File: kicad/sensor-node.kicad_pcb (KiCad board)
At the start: 2 copper layers, 30 x 54 mm, 24 parts

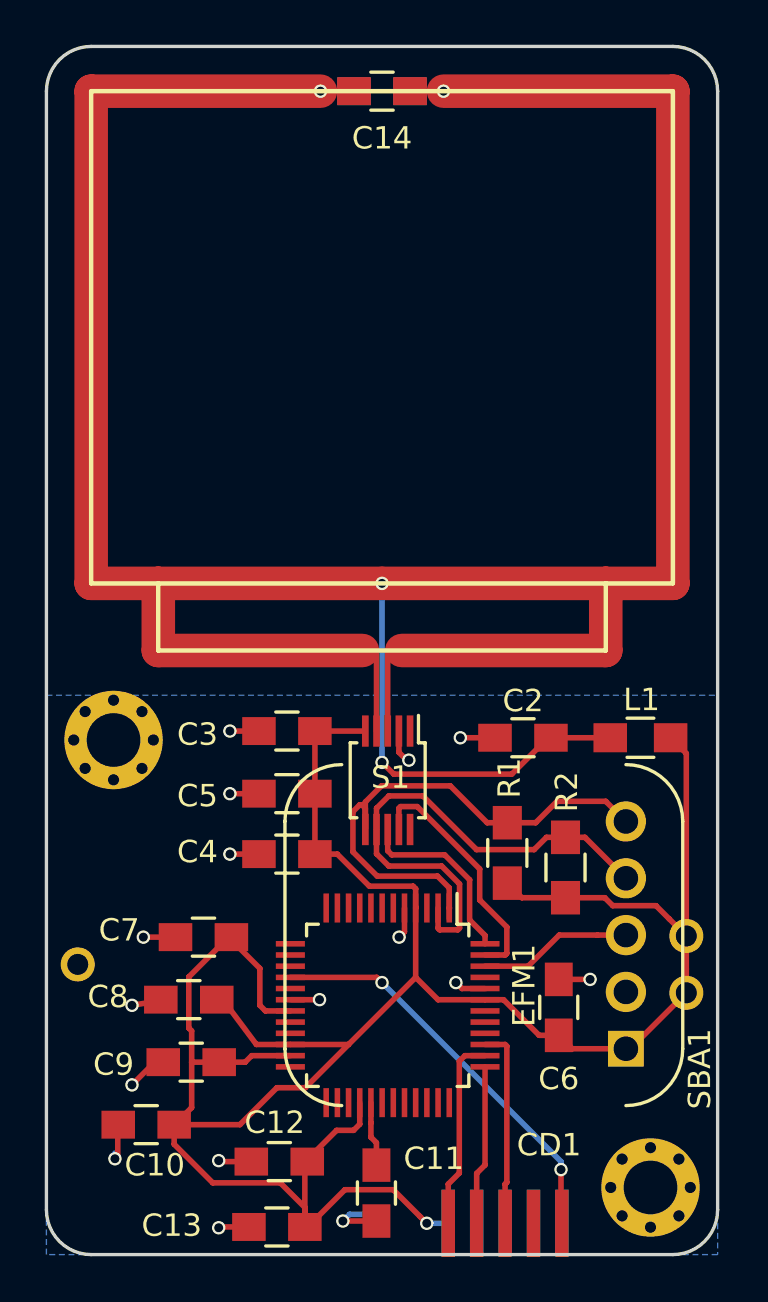
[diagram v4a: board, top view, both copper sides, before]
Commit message: rounded antenna edges
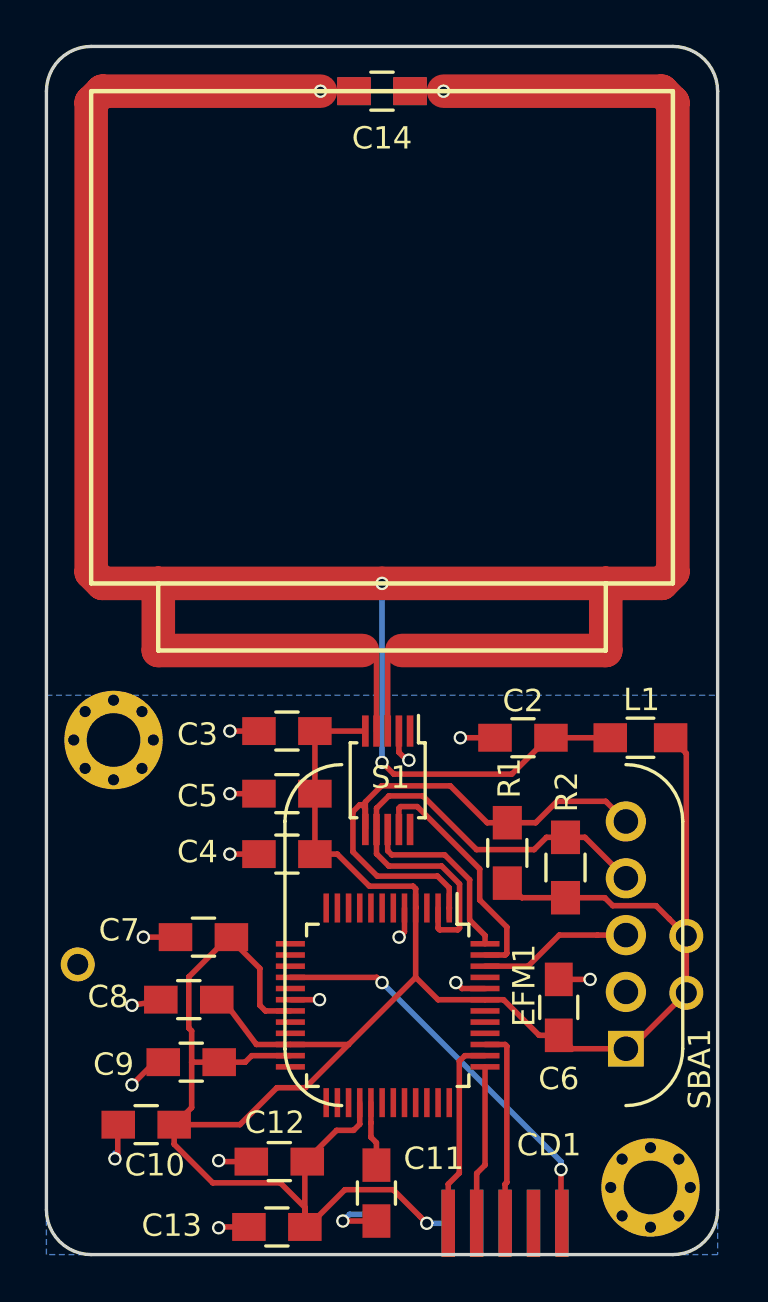
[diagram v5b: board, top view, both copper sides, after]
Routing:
- net Net-(C1-Pad1): track 148.3 -> 147.1 mm
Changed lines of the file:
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@@
     (thickness 1.6)
     (drawings 18)
-    (tracks 238)
+    (tracks 242)
     (zones 0)
     (modules 24)
@@
   (segment (start 142.367 102.87) (end 141.986 102.87) (width 0.25) (layer F.Cu) (net 2))
   (segment (start 141.986 102.87) (end 140.97 103.886) (width 0.25) (layer F.Cu) (net 2))
+  (segment (start 164.646 81.471) (end 165.146 80.971) (width 1.5) (layer F.Cu) (net 3))
+  (segment (start 165.146 59.971) (end 164.646 59.471) (width 1.5) (layer F.Cu) (net 3))
+  (segment (start 139.646 81.471) (end 139.146 80.971) (width 1.5) (layer F.Cu) (net 3))
+  (segment (start 139.146 59.971) (end 139.646 59.471) (width 1.5) (layer F.Cu) (net 3))
   (segment (start 162.346 88.371) (end 159.696 88.371) (width 0.25) (layer F.Cu) (net 3))
   (segment (start 152.4 84.475) (end 153.025 84.475) (width 0.25) (layer F.Cu) (net 3))
@@
   (segment (start 151.9 84.475) (end 151.275 84.475) (width 0.25) (layer F.Cu) (net 3))
   (segment (start 151.275 84.475) (end 151.271 84.471) (width 0.25) (layer F.Cu) (net 3))
-  (segment (start 139.146 59.471) (end 149.396 59.471) (width 1.5) (layer F.Cu) (net 3))
+  (segment (start 139.646 59.471) (end 149.396 59.471) (width 1.5) (layer F.Cu) (net 3))
   (segment (start 149.396 59.471) (end 150.896 59.471) (width 0.25) (layer F.Cu) (net 3))
   (segment (start 150.896 59.471) (end 149.396 59.471) (width 0.25) (layer B.Cu) (net 3))
   (via (at 149.396 59.471) (size 0.6) (drill 0.4) (layers F.Cu B.Cu) (net 3))
-  (segment (start 165.146 59.471) (end 154.896 59.471) (width 1.5) (layer F.Cu) (net 3))
+  (segment (start 164.646 59.471) (end 154.896 59.471) (width 1.5) (layer F.Cu) (net 3))
   (segment (start 154.896 59.471) (end 153.396 59.471) (width 0.25) (layer F.Cu) (net 3))
   (segment (start 153.396 59.471) (end 154.896 59.471) (width 0.25) (layer B.Cu) (net 3))
@@
   (segment (start 152.671001 89.996001) (end 152.146 89.471) (width 0.25) (layer F.Cu) (net 3))
   (via (at 152.146 89.471) (size 0.6) (drill 0.4) (layers F.Cu B.Cu) (net 3))
-  (segment (start 139.146 81.471) (end 139.146 59.471) (width 1.5) (layer F.Cu) (net 3))
-  (segment (start 142.146 81.471) (end 139.146 81.471) (width 1.5) (layer F.Cu) (net 3))
-  (segment (start 165.146 81.471) (end 165.146 59.471) (width 1.5) (layer F.Cu) (net 3))
-  (segment (start 162.146 81.471) (end 165.146 81.471) (width 1.5) (layer F.Cu) (net 3))
+  (segment (start 139.146 80.971) (end 139.146 59.971) (width 1.5) (layer F.Cu) (net 3))
+  (segment (start 142.146 81.471) (end 139.646 81.471) (width 1.5) (layer F.Cu) (net 3))
+  (segment (start 165.146 80.971) (end 165.146 59.971) (width 1.5) (layer F.Cu) (net 3))
+  (segment (start 162.146 81.471) (end 164.646 81.471) (width 1.5) (layer F.Cu) (net 3))
   (segment (start 162.146 84.471) (end 162.146 81.471) (width 1.5) (layer F.Cu) (net 3))
   (segment (start 153.029 84.471) (end 162.146 84.471) (width 1.5) (layer F.Cu) (net 3))

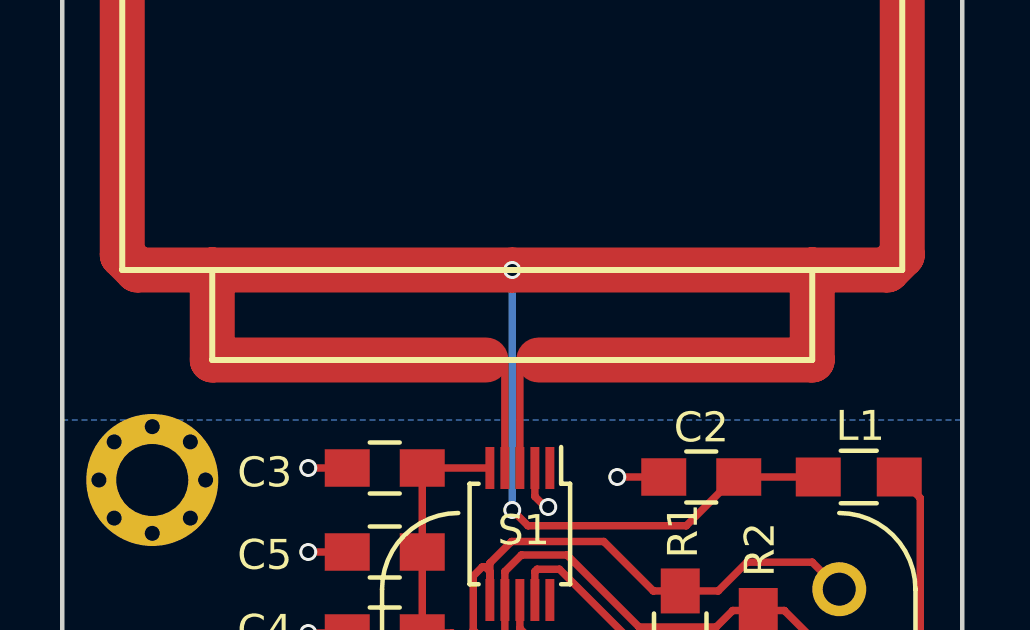
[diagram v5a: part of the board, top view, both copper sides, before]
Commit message: refined feed loop size
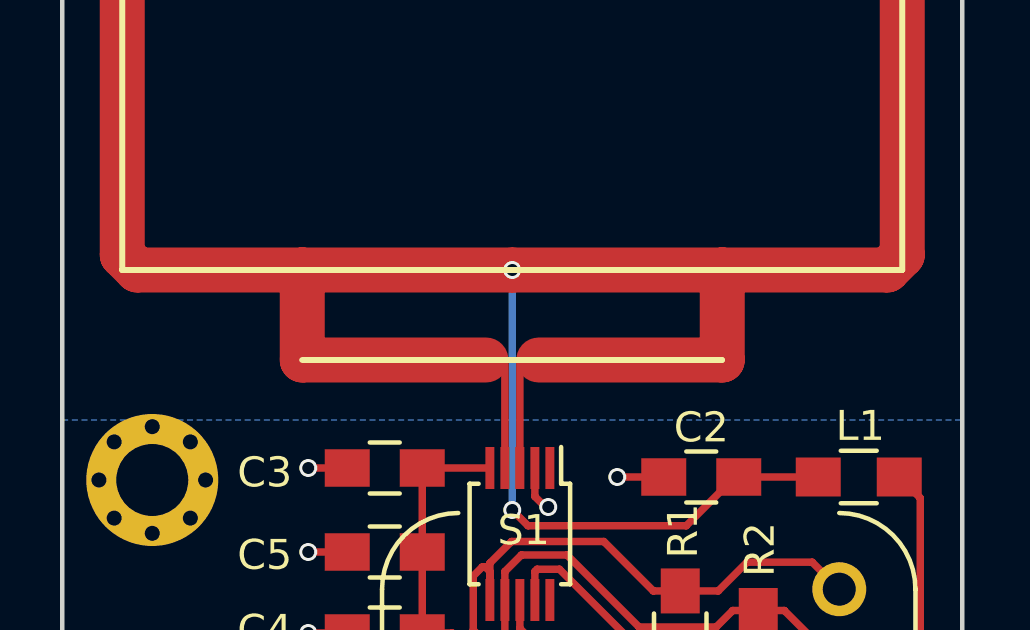
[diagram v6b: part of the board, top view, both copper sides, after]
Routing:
- net Net-(C1-Pad1): track 147.1 -> 141.1 mm
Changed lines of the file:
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@@
     (area 124.24918 56.396 179.995999 119.171001)
     (thickness 1.6)
-    (drawings 18)
+    (drawings 16)
     (tracks 242)
     (zones 0)
@@
     (arrow2b (pts (xy 172.145999 57.471) (xy 172.73242 58.597504)))
   )
-  (gr_line (start 142.146 84.471) (end 142.146 81.471) (layer F.SilkS) (width 0.2))
-  (gr_line (start 162.146 84.471) (end 142.146 84.471) (layer F.SilkS) (width 0.2))
-  (gr_line (start 162.146 81.471) (end 162.146 84.471) (layer F.SilkS) (width 0.2))
+  (gr_line (start 159.146 84.471) (end 145.146 84.471) (layer F.SilkS) (width 0.2))
   (gr_line (start 139.146 81.471) (end 139.146 59.471) (layer F.SilkS) (width 0.2))
   (gr_line (start 165.146 81.471) (end 139.146 81.471) (layer F.SilkS) (width 0.2))
@@
   (segment (start 153.396 59.471) (end 154.896 59.471) (width 0.25) (layer B.Cu) (net 3))
   (via (at 154.896 59.471) (size 0.6) (drill 0.4) (layers F.Cu B.Cu) (net 3))
-  (segment (start 142.146 81.471) (end 152.146 81.471) (width 1.5) (layer F.Cu) (net 3))
-  (segment (start 152.146 81.471) (end 162.146 81.471) (width 1.5) (layer F.Cu) (net 3))
+  (segment (start 145.146 81.471) (end 152.146 81.471) (width 1.5) (layer F.Cu) (net 3))
+  (segment (start 152.146 81.471) (end 159.146 81.471) (width 1.5) (layer F.Cu) (net 3))
   (segment (start 152.146 89.471) (end 152.146 81.471) (width 0.25) (layer B.Cu) (net 3))
   (via (at 152.146 81.471) (size 0.6) (drill 0.4) (layers F.Cu B.Cu) (net 3))
@@
   (via (at 152.146 89.471) (size 0.6) (drill 0.4) (layers F.Cu B.Cu) (net 3))
   (segment (start 139.146 80.971) (end 139.146 59.971) (width 1.5) (layer F.Cu) (net 3))
-  (segment (start 142.146 81.471) (end 139.646 81.471) (width 1.5) (layer F.Cu) (net 3))
+  (segment (start 145.146 81.471) (end 139.646 81.471) (width 1.5) (layer F.Cu) (net 3))
   (segment (start 165.146 80.971) (end 165.146 59.971) (width 1.5) (layer F.Cu) (net 3))
-  (segment (start 162.146 81.471) (end 164.646 81.471) (width 1.5) (layer F.Cu) (net 3))
-  (segment (start 162.146 84.471) (end 162.146 81.471) (width 1.5) (layer F.Cu) (net 3))
-  (segment (start 153.029 84.471) (end 162.146 84.471) (width 1.5) (layer F.Cu) (net 3))
+  (segment (start 159.146 81.471) (end 164.646 81.471) (width 1.5) (layer F.Cu) (net 3))
+  (segment (start 159.146 84.471) (end 159.146 81.471) (width 1.5) (layer F.Cu) (net 3))
+  (segment (start 153.029 84.471) (end 159.146 84.471) (width 1.5) (layer F.Cu) (net 3))
   (segment (start 152.4 84.475) (end 152.404 84.471) (width 0.25) (layer F.Cu) (net 3))
   (segment (start 152.4 88.071) (end 152.4 84.475) (width 0.25) (layer F.Cu) (net 3))
-  (segment (start 142.146 84.471) (end 142.146 81.471) (width 1.5) (layer F.Cu) (net 3))
-  (segment (start 151.271 84.471) (end 142.146 84.471) (width 1.5) (layer F.Cu) (net 3))
+  (segment (start 145.146 84.471) (end 145.146 81.471) (width 1.5) (layer F.Cu) (net 3))
+  (segment (start 151.271 84.471) (end 145.146 84.471) (width 1.5) (layer F.Cu) (net 3))
   (segment (start 151.9 84.475) (end 151.896 84.471) (width 0.25) (layer F.Cu) (net 3))
   (segment (start 151.9 88.071) (end 151.9 84.475) (width 0.25) (layer F.Cu) (net 3))

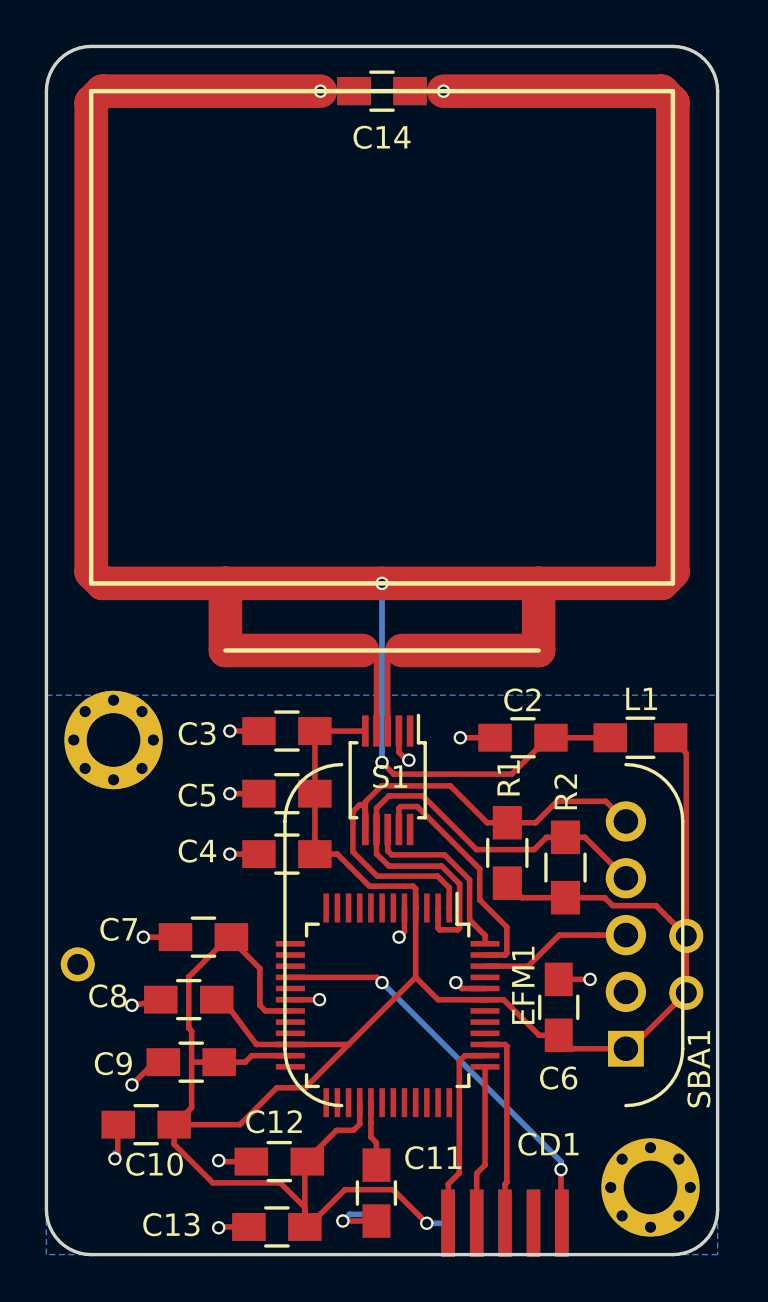
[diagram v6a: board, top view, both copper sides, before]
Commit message: added a decoupling capacitor
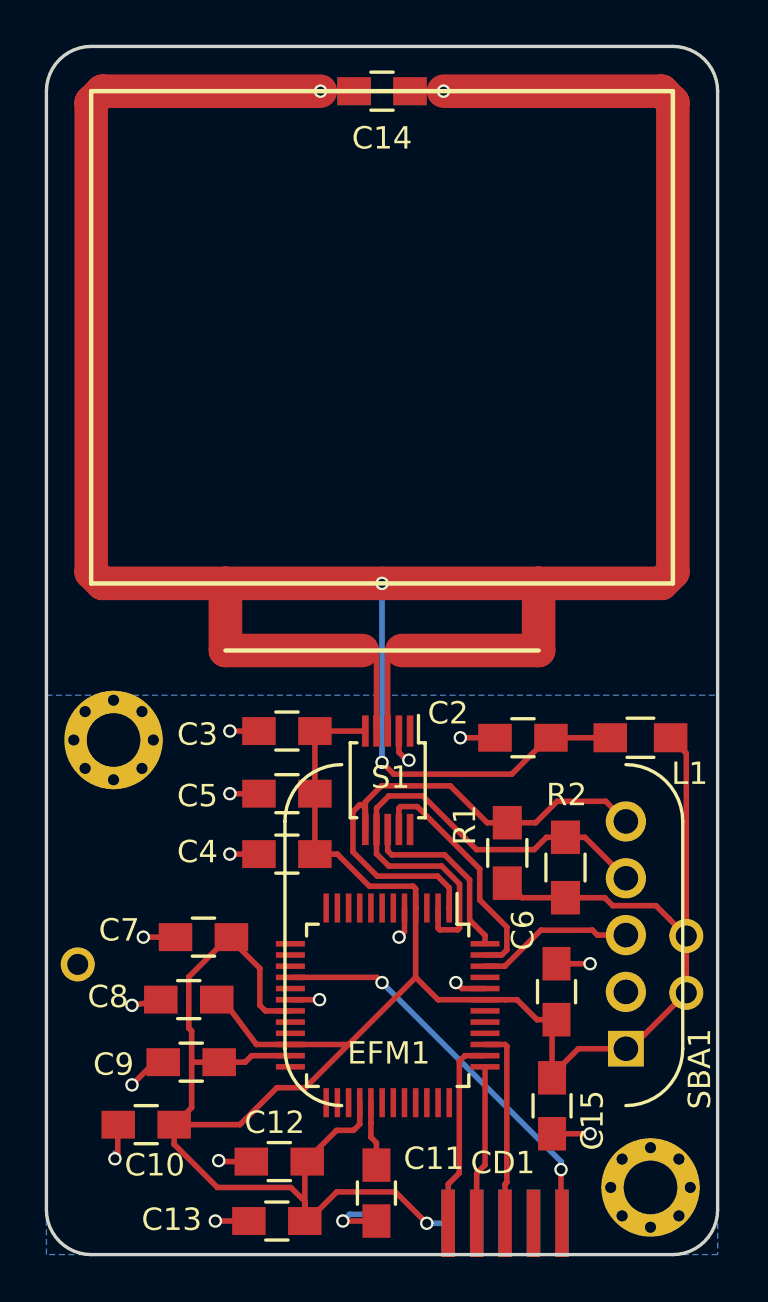
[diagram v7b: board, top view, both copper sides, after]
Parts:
- added C15: 10µF, Capacitors_SMD:C_0805_HandSoldering, F.Cu at (159.7, 104.8)
- moved C6 0.71 mm to (159.9, 99.7)
- moved C13 0.27 mm to (147.4, 110.0)
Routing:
- net +3V3: track 116.0 -> 119.0 mm
- net GND: track 24.8 -> 26.7 mm, vias 16 -> 17

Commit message: improved silk screen decoration
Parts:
- added G***: LOGO, sensor-node-main:logo, F.Cu at (152.1, 70.5)
- added G***: LOGO, sensor-node-main:frequ, F.Cu at (152.1, 83.0)
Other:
- board text added: "www.hochreiner.net sensor node V1.0.0"
